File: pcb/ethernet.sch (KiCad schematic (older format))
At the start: 37 parts, among them U5 KSZ9031RN, U8 DSC6001HI2A-025.0000

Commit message: Assigned lots of footprints. Still have a few to go.
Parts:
- C24, C25, C26, C30, C31, C32: footprint (none) -> azonenberg_pcb:EIA_0603_CAP_NOSILK
- C27, C28, C29, C33, C34, C35, C36, C37, C38, C39, C40, C41, C42, C43: footprint (none) -> azonenberg_pcb:EIA_0402_CAP_NOSILK
- R10, R11, R12, R13, R2, R3, R4, R5, R6, R7, R8, R9: footprint (none) -> azonenberg_pcb:EIA_0402_RES_NOSILK
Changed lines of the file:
@@
 F 0 "R4" H 4720 1646 50  0000 L CNN
 F 1 "1K" H 4720 1555 50  0000 L CNN
-F 2 "" V 4580 1600 50  0001 C CNN
+F 2 "azonenberg_pcb:EIA_0402_RES_NOSILK" V 4580 1600 50  0001 C CNN
 F 3 "" H 4650 1600 50  0001 C CNN
 	1    4650 1600
@@
 F 0 "R3" H 4720 1246 50  0000 L CNN
 F 1 "1K" H 4720 1155 50  0000 L CNN
-F 2 "" V 4580 1200 50  0001 C CNN
+F 2 "azonenberg_pcb:EIA_0402_RES_NOSILK" V 4580 1200 50  0001 C CNN
 F 3 "" H 4650 1200 50  0001 C CNN
 	1    4650 1200
@@
 F 0 "R2" V 4200 3950 50  0000 C CNN
 F 1 "12.1K 1%" V 4400 4000 50  0000 C CNN
-F 2 "" V 4230 3950 50  0001 C CNN
+F 2 "azonenberg_pcb:EIA_0402_RES_NOSILK" V 4230 3950 50  0001 C CNN
 F 3 "" H 4300 3950 50  0001 C CNN
 	1    4300 3950
@@
 F 0 "R5" V 4700 3450 50  0000 C CNN
 F 1 "10K" V 4750 3300 50  0000 C CNN
-F 2 "" V 4680 3300 50  0001 C CNN
+F 2 "azonenberg_pcb:EIA_0402_RES_NOSILK" V 4680 3300 50  0001 C CNN
 F 3 "" H 4750 3300 50  0001 C CNN
 	1    4750 3300
@@
 F 0 "R8" V 9000 1200 50  0000 C CNN
 F 1 "10K" V 9050 1050 50  0000 C CNN
-F 2 "" V 8980 1050 50  0001 C CNN
+F 2 "azonenberg_pcb:EIA_0402_RES_NOSILK" V 8980 1050 50  0001 C CNN
 F 3 "" H 9050 1050 50  0001 C CNN
 	1    9050 1050
@@
 F 0 "R9" V 9000 1300 50  0000 C CNN
 F 1 "10K" V 9050 1150 50  0000 C CNN
-F 2 "" V 8980 1150 50  0001 C CNN
+F 2 "azonenberg_pcb:EIA_0402_RES_NOSILK" V 8980 1150 50  0001 C CNN
 F 3 "" H 9050 1150 50  0001 C CNN
 	1    9050 1150
@@
 F 0 "R10" V 9000 1400 50  0000 C CNN
 F 1 "10K" V 9050 1250 50  0000 C CNN
-F 2 "" V 8980 1250 50  0001 C CNN
+F 2 "azonenberg_pcb:EIA_0402_RES_NOSILK" V 8980 1250 50  0001 C CNN
 F 3 "" H 9050 1250 50  0001 C CNN
 	1    9050 1250
@@
 F 0 "R11" V 9000 1500 50  0000 C CNN
 F 1 "10K" V 9050 1350 50  0000 C CNN
-F 2 "" V 8980 1350 50  0001 C CNN
+F 2 "azonenberg_pcb:EIA_0402_RES_NOSILK" V 8980 1350 50  0001 C CNN
 F 3 "" H 9050 1350 50  0001 C CNN
 	1    9050 1350
@@
 F 0 "R12" V 9000 1850 50  0000 C CNN
 F 1 "10K" V 9050 1700 50  0000 C CNN
-F 2 "" V 8980 1700 50  0001 C CNN
+F 2 "azonenberg_pcb:EIA_0402_RES_NOSILK" V 8980 1700 50  0001 C CNN
 F 3 "" H 9050 1700 50  0001 C CNN
 	1    9050 1700
@@
 F 0 "U8" H 6125 4037 60  0000 C CNN
 F 1 "DSC6001HI2A-025.0000" H 6125 3931 60  0000 C CNN
-F 2 "" H 6150 3750 60  0000 C CNN
+F 2 "" H 6150 3750 60  0001 C CNN
 F 3 "" H 6150 3750 60  0000 C CNN
 	1    6150 3750
@@
 F 0 "R7" V 5150 3900 50  0000 C CNN
 F 1 "33" V 5200 3750 50  0000 C CNN
-F 2 "" V 5130 3750 50  0001 C CNN
+F 2 "azonenberg_pcb:EIA_0402_RES_NOSILK" V 5130 3750 50  0001 C CNN
 F 3 "" H 5200 3750 50  0001 C CNN
 	1    5200 3750
@@
 F 0 "C43" H 7365 3896 50  0000 L CNN
 F 1 "0.47 uF" H 7365 3805 50  0000 L CNN
-F 2 "" H 7288 3700 50  0001 C CNN
+F 2 "azonenberg_pcb:EIA_0402_CAP_NOSILK" H 7288 3700 50  0001 C CNN
 F 3 "" H 7250 3850 50  0001 C CNN
 	1    7250 3850
@@
 F 0 "R13" V 9000 2200 50  0000 C CNN
 F 1 "10K" V 9050 2050 50  0000 C CNN
-F 2 "" V 8980 2050 50  0001 C CNN
+F 2 "azonenberg_pcb:EIA_0402_RES_NOSILK" V 8980 2050 50  0001 C CNN
 F 3 "" H 9050 2050 50  0001 C CNN
 	1    9050 2050
@@
 F 0 "FB1" V 1342 5000 40  0000 C CNN
 F 1 "INDUCTOR_PWROUT" V 1418 5000 40  0000 C CNN
-F 2 "" H 1500 5000 60  0000 C CNN
+F 2 "" H 1500 5000 60  0001 C CNN
 F 3 "" H 1500 5000 60  0000 C CNN
 	1    1500 5000
@@
 F 0 "C24" H 1115 5196 50  0000 L CNN
 F 1 "4.7 uF" H 1115 5105 50  0000 L CNN
-F 2 "" H 1038 5000 50  0001 C CNN
+F 2 "azonenberg_pcb:EIA_0603_CAP_NOSILK" H 1038 5000 50  0001 C CNN
 F 3 "" H 1000 5150 50  0001 C CNN
 	1    1000 5150
@@
 F 0 "C30" H 2015 5196 50  0000 L CNN
 F 1 "4.7 uF" H 2015 5105 50  0000 L CNN
-F 2 "" H 1938 5000 50  0001 C CNN
+F 2 "azonenberg_pcb:EIA_0603_CAP_NOSILK" H 1938 5000 50  0001 C CNN
 F 3 "" H 1900 5150 50  0001 C CNN
 	1    1900 5150
@@
 F 0 "C35" H 2565 5196 50  0000 L CNN
 F 1 "0.47 uF" H 2565 5105 50  0000 L CNN
-F 2 "" H 2488 5000 50  0001 C CNN
+F 2 "azonenberg_pcb:EIA_0402_CAP_NOSILK" H 2488 5000 50  0001 C CNN
 F 3 "" H 2450 5150 50  0001 C CNN
 	1    2450 5150
@@
 F 0 "C39" H 3115 5196 50  0000 L CNN
 F 1 "0.47 uF" H 3115 5105 50  0000 L CNN
-F 2 "" H 3038 5000 50  0001 C CNN
+F 2 "azonenberg_pcb:EIA_0402_CAP_NOSILK" H 3038 5000 50  0001 C CNN
 F 3 "" H 3000 5150 50  0001 C CNN
 	1    3000 5150
@@
 F 0 "C25" H 1115 5696 50  0000 L CNN
 F 1 "4.7 uF" H 1115 5605 50  0000 L CNN
-F 2 "" H 1038 5500 50  0001 C CNN
+F 2 "azonenberg_pcb:EIA_0603_CAP_NOSILK" H 1038 5500 50  0001 C CNN
 F 3 "" H 1000 5650 50  0001 C CNN
 	1    1000 5650
@@
 F 0 "C28" H 1665 5696 50  0000 L CNN
 F 1 "0.47 uF" H 1665 5605 50  0000 L CNN
-F 2 "" H 1588 5500 50  0001 C CNN
+F 2 "azonenberg_pcb:EIA_0402_CAP_NOSILK" H 1588 5500 50  0001 C CNN
 F 3 "" H 1550 5650 50  0001 C CNN
 	1    1550 5650
@@
 F 0 "C33" H 2215 5696 50  0000 L CNN
 F 1 "0.47 uF" H 2215 5605 50  0000 L CNN
-F 2 "" H 2138 5500 50  0001 C CNN
+F 2 "azonenberg_pcb:EIA_0402_CAP_NOSILK" H 2138 5500 50  0001 C CNN
 F 3 "" H 2100 5650 50  0001 C CNN
 	1    2100 5650
@@
 F 0 "FB2" V 1342 6000 40  0000 C CNN
 F 1 "INDUCTOR_PWROUT" V 1418 6000 40  0000 C CNN
-F 2 "" H 1500 6000 60  0000 C CNN
+F 2 "" H 1500 6000 60  0001 C CNN
 F 3 "" H 1500 6000 60  0000 C CNN
 	1    1500 6000
@@
 F 0 "C26" H 1115 6196 50  0000 L CNN
 F 1 "4.7 uF" H 1115 6105 50  0000 L CNN
-F 2 "" H 1038 6000 50  0001 C CNN
+F 2 "azonenberg_pcb:EIA_0603_CAP_NOSILK" H 1038 6000 50  0001 C CNN
 F 3 "" H 1000 6150 50  0001 C CNN
 	1    1000 6150
@@
 F 0 "C31" H 2015 6196 50  0000 L CNN
 F 1 "4.7 uF" H 2015 6105 50  0000 L CNN
-F 2 "" H 1938 6000 50  0001 C CNN
+F 2 "azonenberg_pcb:EIA_0603_CAP_NOSILK" H 1938 6000 50  0001 C CNN
 F 3 "" H 1900 6150 50  0001 C CNN
 	1    1900 6150
@@
 F 0 "C36" H 2565 6196 50  0000 L CNN
 F 1 "0.47 uF" H 2565 6105 50  0000 L CNN
-F 2 "" H 2488 6000 50  0001 C CNN
+F 2 "azonenberg_pcb:EIA_0402_CAP_NOSILK" H 2488 6000 50  0001 C CNN
 F 3 "" H 2450 6150 50  0001 C CNN
 	1    2450 6150
@@
 F 0 "C40" H 3115 6196 50  0000 L CNN
 F 1 "0.47 uF" H 3115 6105 50  0000 L CNN
-F 2 "" H 3038 6000 50  0001 C CNN
+F 2 "azonenberg_pcb:EIA_0402_CAP_NOSILK" H 3038 6000 50  0001 C CNN
 F 3 "" H 3000 6150 50  0001 C CNN
 	1    3000 6150
@@
 F 0 "FB3" V 1342 6550 40  0000 C CNN
 F 1 "INDUCTOR_PWROUT" V 1418 6550 40  0000 C CNN
-F 2 "" H 1500 6550 60  0000 C CNN
+F 2 "" H 1500 6550 60  0001 C CNN
 F 3 "" H 1500 6550 60  0000 C CNN
 	1    1500 6550
@@
 F 0 "C32" H 2015 6746 50  0000 L CNN
 F 1 "4.7 uF" H 2015 6655 50  0000 L CNN
-F 2 "" H 1938 6550 50  0001 C CNN
+F 2 "azonenberg_pcb:EIA_0603_CAP_NOSILK" H 1938 6550 50  0001 C CNN
 F 3 "" H 1900 6700 50  0001 C CNN
 	1    1900 6700
@@
 F 0 "C37" H 2565 6746 50  0000 L CNN
 F 1 "0.47 uF" H 2565 6655 50  0000 L CNN
-F 2 "" H 2488 6550 50  0001 C CNN
+F 2 "azonenberg_pcb:EIA_0402_CAP_NOSILK" H 2488 6550 50  0001 C CNN
 F 3 "" H 2450 6700 50  0001 C CNN
 	1    2450 6700
@@
 F 0 "C27" H 1115 7296 50  0000 L CNN
 F 1 "0.47 uF" H 1115 7205 50  0000 L CNN
-F 2 "" H 1038 7100 50  0001 C CNN
+F 2 "azonenberg_pcb:EIA_0402_CAP_NOSILK" H 1038 7100 50  0001 C CNN
 F 3 "" H 1000 7250 50  0001 C CNN
 	1    1000 7250
@@
 F 0 "C29" H 1665 7296 50  0000 L CNN
 F 1 "0.47 uF" H 1665 7205 50  0000 L CNN
-F 2 "" H 1588 7100 50  0001 C CNN
+F 2 "azonenberg_pcb:EIA_0402_CAP_NOSILK" H 1588 7100 50  0001 C CNN
 F 3 "" H 1550 7250 50  0001 C CNN
 	1    1550 7250
@@
 F 0 "C34" H 2265 7296 50  0000 L CNN
 F 1 "0.47 uF" H 2265 7205 50  0000 L CNN
-F 2 "" H 2188 7100 50  0001 C CNN
+F 2 "azonenberg_pcb:EIA_0402_CAP_NOSILK" H 2188 7100 50  0001 C CNN
 F 3 "" H 2150 7250 50  0001 C CNN
 	1    2150 7250
@@
 F 0 "C38" H 2865 7296 50  0000 L CNN
 F 1 "0.47 uF" H 2865 7205 50  0000 L CNN
-F 2 "" H 2788 7100 50  0001 C CNN
+F 2 "azonenberg_pcb:EIA_0402_CAP_NOSILK" H 2788 7100 50  0001 C CNN
 F 3 "" H 2750 7250 50  0001 C CNN
 	1    2750 7250
@@
 F 0 "C41" H 3465 7296 50  0000 L CNN
 F 1 "0.47 uF" H 3465 7205 50  0000 L CNN
-F 2 "" H 3388 7100 50  0001 C CNN
+F 2 "azonenberg_pcb:EIA_0402_CAP_NOSILK" H 3388 7100 50  0001 C CNN
 F 3 "" H 3350 7250 50  0001 C CNN
 	1    3350 7250
@@
 F 0 "C42" H 4015 7296 50  0000 L CNN
 F 1 "0.47 uF" H 4015 7205 50  0000 L CNN
-F 2 "" H 3938 7100 50  0001 C CNN
+F 2 "azonenberg_pcb:EIA_0402_CAP_NOSILK" H 3938 7100 50  0001 C CNN
 F 3 "" H 3900 7250 50  0001 C CNN
 	1    3900 7250
@@
 F 0 "R6" V 4950 2950 50  0000 C CNN
 F 1 "1K" V 5050 2950 50  0000 C CNN
-F 2 "" V 4980 2950 50  0001 C CNN
+F 2 "azonenberg_pcb:EIA_0402_RES_NOSILK" V 4980 2950 50  0001 C CNN
 F 3 "" H 5050 2950 50  0001 C CNN
 	1    5050 2950

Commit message: Finished initial footprint assignments
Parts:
- FB1, FB2, FB3: value INDUCTOR_PWROUT -> 600R @ 100 MHz; footprint (none) -> azonenberg_pcb:EIA_0402_CAP_NOSILK
- U8: footprint (none) -> azonenberg_pcb:OSCILLATOR_1.6x1.2
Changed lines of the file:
@@
 F 0 "U8" H 6125 4037 60  0000 C CNN
 F 1 "DSC6001HI2A-025.0000" H 6125 3931 60  0000 C CNN
-F 2 "" H 6150 3750 60  0001 C CNN
+F 2 "azonenberg_pcb:OSCILLATOR_1.6x1.2" H 6150 3750 60  0001 C CNN
 F 3 "" H 6150 3750 60  0000 C CNN
 	1    6150 3750
@@
 P 1500 5000
 F 0 "FB1" V 1342 5000 40  0000 C CNN
-F 1 "INDUCTOR_PWROUT" V 1418 5000 40  0000 C CNN
-F 2 "" H 1500 5000 60  0001 C CNN
+F 1 "600R @ 100 MHz" V 1418 5000 40  0000 C CNN
+F 2 "azonenberg_pcb:EIA_0402_CAP_NOSILK" H 1500 5000 60  0001 C CNN
 F 3 "" H 1500 5000 60  0000 C CNN
 	1    1500 5000
@@
 P 1500 6000
 F 0 "FB2" V 1342 6000 40  0000 C CNN
-F 1 "INDUCTOR_PWROUT" V 1418 6000 40  0000 C CNN
-F 2 "" H 1500 6000 60  0001 C CNN
+F 1 "600R @ 100 MHz" V 1418 6000 40  0000 C CNN
+F 2 "azonenberg_pcb:EIA_0402_CAP_NOSILK" H 1500 6000 60  0001 C CNN
 F 3 "" H 1500 6000 60  0000 C CNN
 	1    1500 6000
@@
 P 1500 6550
 F 0 "FB3" V 1342 6550 40  0000 C CNN
-F 1 "INDUCTOR_PWROUT" V 1418 6550 40  0000 C CNN
-F 2 "" H 1500 6550 60  0001 C CNN
+F 1 "600R @ 100 MHz" V 1418 6550 40  0000 C CNN
+F 2 "azonenberg_pcb:EIA_0402_CAP_NOSILK" H 1500 6550 60  0001 C CNN
 F 3 "" H 1500 6550 60  0000 C CNN
 	1    1500 6550

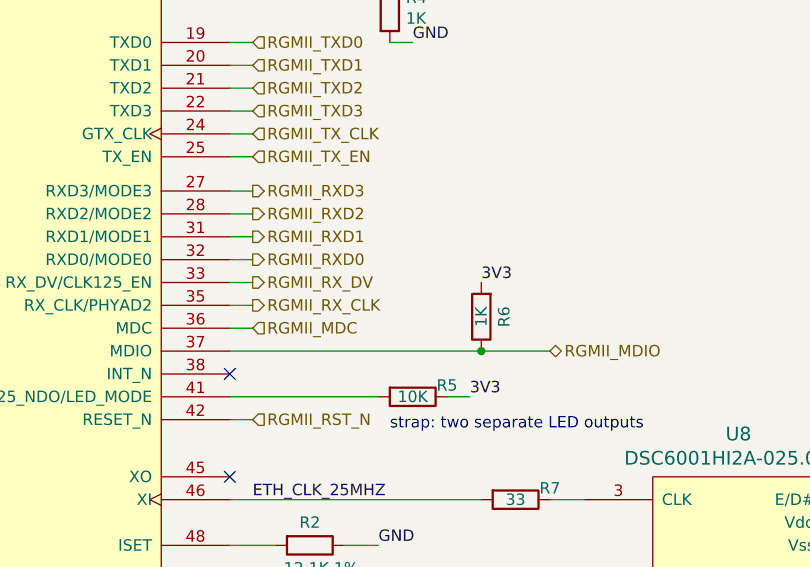
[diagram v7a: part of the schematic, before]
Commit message: Continued FPGA layout. Fanned out most signals going to MCU but pin assignments aren't final.
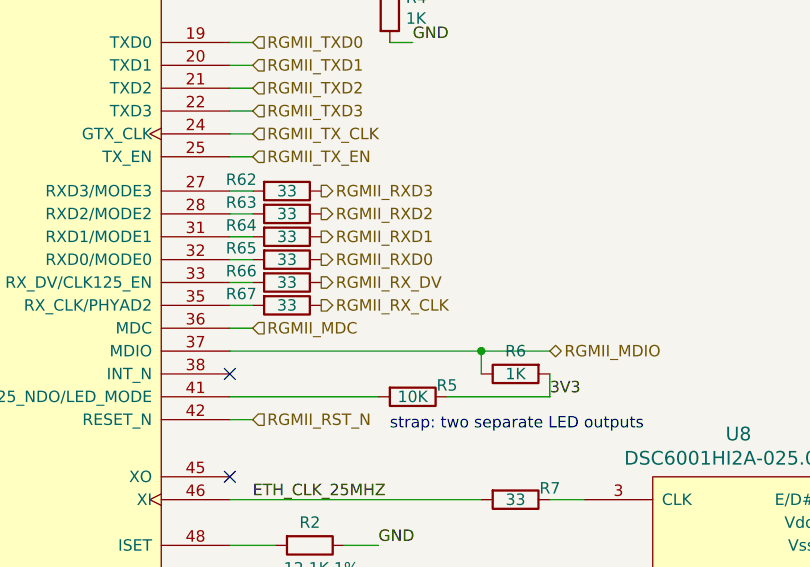
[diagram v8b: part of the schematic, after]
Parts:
- added R62, R63, R64, R65, R66, R67: 33, azonenberg_pcb:EIA_0402_RES_NOSILK, symbol device:R
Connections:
- net RGMII_RXD0: now also R65.1; no longer U5.32 (RXD0/MODE0)
- net RGMII_RXD1: now also R64.1; no longer U5.31 (RXD1/MODE1)
- net RGMII_RXD2: now also R63.1; no longer U5.28 (RXD2/MODE2)
- net RGMII_RXD3: now also R62.1; no longer U5.27 (RXD3/MODE3)
- net RGMII_RX_CLK: now also R67.1; no longer U5.35 (RX_CLK/PHYAD2)
- net RGMII_RX_DV: now also R66.1; no longer U5.33 (RX_DV/CLK125_EN)
- new net: R62.2, U5.27 (RXD3/MODE3)
- new net: R63.2, U5.28 (RXD2/MODE2)
- new net: R64.2, U5.31 (RXD1/MODE1)
- new net: R65.2, U5.32 (RXD0/MODE0)
- new net: R66.2, U5.33 (RX_DV/CLK125_EN)
- new net: R67.2, U5.35 (RX_CLK/PHYAD2)
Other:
- moved on the sheet: R6
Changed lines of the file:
@@
 Sheet 5 8
 Title "INTEGRALSTICK Compute Module"
-Date "2018-11-13"
+Date "2018-11-14"
 Rev "0.1"
 Comp "Andrew D. Zonenberg"
@@
 Wire Wire Line
 	4050 1750 3950 1750
-Text HLabel 4050 2400 2    50   Output ~ 0
+Text HLabel 4350 2400 2    50   Output ~ 0
 RGMII_RXD3
-Text HLabel 4050 2500 2    50   Output ~ 0
+Text HLabel 4350 2500 2    50   Output ~ 0
 RGMII_RXD2
-Text HLabel 4050 2600 2    50   Output ~ 0
+Text HLabel 4350 2600 2    50   Output ~ 0
 RGMII_RXD1
-Text HLabel 4050 2700 2    50   Output ~ 0
+Text HLabel 4350 2700 2    50   Output ~ 0
 RGMII_RXD0
-Text HLabel 4050 2800 2    50   Output ~ 0
+Text HLabel 4350 2800 2    50   Output ~ 0
 RGMII_RX_DV
-Text HLabel 4050 2900 2    50   Output ~ 0
+Text HLabel 4350 2900 2    50   Output ~ 0
 RGMII_RX_CLK
 Text HLabel 4050 3000 2    50   Input ~ 0
@@
 Wire Wire Line
 	3950 3300 4600 3300
-Text Label 5000 3300 0    50   ~ 0
+Text Label 5350 3300 0    50   ~ 0
 3V3
-Wire Wire Line
-	5000 3300 4900 3300
 $Comp
 L device:R R8
@@
 Wire Wire Line
 	3350 7400 2750 7400
-Wire Wire Line
-	3950 3100 5050 3100
 $Comp
 L device:R R6
 U 1 1 5BEF5A2A
-P 5050 2950
-F 0 "R6" V 4950 2950 50  0000 C CNN
-F 1 "1K" V 5050 2950 50  0000 C CNN
-F 2 "azonenberg_pcb:EIA_0402_RES_NOSILK" V 4980 2950 50  0001 C CNN
-F 3 "" H 5050 2950 50  0001 C CNN
-	1    5050 2950
-	-1   0    0    1
-$EndComp
-Connection ~ 5050 3100
-Wire Wire Line
-	5050 3100 5350 3100
-Text Label 5050 2800 0    50   ~ 0
-3V3
+P 5200 3200
+F 0 "R6" V 5100 3200 50  0000 C CNN
+F 1 "1K" V 5200 3200 50  0000 C CNN
+F 2 "azonenberg_pcb:EIA_0402_RES_NOSILK" V 5130 3200 50  0001 C CNN
+F 3 "" H 5200 3200 50  0001 C CNN
+	1    5200 3200
+	0    -1   1    0
+$EndComp
 Text HLabel 1000 5000 0    50   Input ~ 0
 2V5
 Text Label 4050 3750 0    50   ~ 0
 ETH_CLK_25MHZ
+Wire Wire Line
+	3950 3100 5050 3100
+Wire Wire Line
+	5050 3200 5050 3100
+Connection ~ 5050 3100
+Wire Wire Line
+	5050 3100 5350 3100
+Wire Wire Line
+	5350 3300 5350 3200
+Wire Wire Line
+	4900 3300 5350 3300
+$Comp
+L device:R R62
+U 1 1 5C46B5A3
+P 4200 2400
+F 0 "R62" V 4150 2200 50  0000 C CNN
+F 1 "33" V 4200 2400 50  0000 C CNN
+F 2 "azonenberg_pcb:EIA_0402_RES_NOSILK" V 4130 2400 50  0001 C CNN
+F 3 "" H 4200 2400 50  0001 C CNN
+	1    4200 2400
+	0    1    1    0
+$EndComp
+$Comp
+L device:R R63
+U 1 1 5C471F48
+P 4200 2500
+F 0 "R63" V 4150 2300 50  0000 C CNN
+F 1 "33" V 4200 2500 50  0000 C CNN
+F 2 "azonenberg_pcb:EIA_0402_RES_NOSILK" V 4130 2500 50  0001 C CNN
+F 3 "" H 4200 2500 50  0001 C CNN
+	1    4200 2500
+	0    1    1    0
+$EndComp
+$Comp
+L device:R R64
+U 1 1 5C472432
+P 4200 2600
+F 0 "R64" V 4150 2400 50  0000 C CNN
+F 1 "33" V 4200 2600 50  0000 C CNN
+F 2 "azonenberg_pcb:EIA_0402_RES_NOSILK" V 4130 2600 50  0001 C CNN
+F 3 "" H 4200 2600 50  0001 C CNN
+	1    4200 2600
+	0    1    1    0
+$EndComp
+$Comp
+L device:R R65
+U 1 1 5C4727BD
+P 4200 2700
+F 0 "R65" V 4150 2500 50  0000 C CNN
+F 1 "33" V 4200 2700 50  0000 C CNN
+F 2 "azonenberg_pcb:EIA_0402_RES_NOSILK" V 4130 2700 50  0001 C CNN
+F 3 "" H 4200 2700 50  0001 C CNN
+	1    4200 2700
+	0    1    1    0
+$EndComp
+$Comp
+L device:R R66
+U 1 1 5C472B4C
+P 4200 2800
+F 0 "R66" V 4150 2600 50  0000 C CNN
+F 1 "33" V 4200 2800 50  0000 C CNN
+F 2 "azonenberg_pcb:EIA_0402_RES_NOSILK" V 4130 2800 50  0001 C CNN
+F 3 "" H 4200 2800 50  0001 C CNN
+	1    4200 2800
+	0    1    1    0
+$EndComp
+$Comp
+L device:R R67
+U 1 1 5C472F18
+P 4200 2900
+F 0 "R67" V 4150 2700 50  0000 C CNN
+F 1 "33" V 4200 2900 50  0000 C CNN
+F 2 "azonenberg_pcb:EIA_0402_RES_NOSILK" V 4130 2900 50  0001 C CNN
+F 3 "" H 4200 2900 50  0001 C CNN
+	1    4200 2900
+	0    1    1    0
+$EndComp
 $EndSCHEMATC
